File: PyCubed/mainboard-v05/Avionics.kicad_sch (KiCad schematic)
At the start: 33 parts, among them SW1 KMR231NG LFS, U1 MAX706RESA, U2 ATSAMD51J19A-AU, U3 BMX160, Y1 32.768kHz

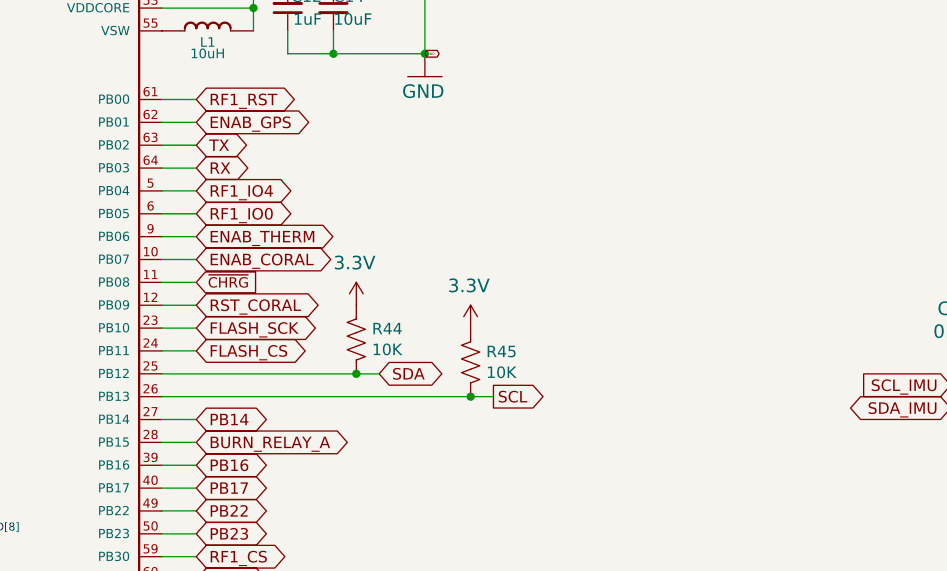
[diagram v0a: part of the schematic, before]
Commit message: final updates after JLC i2c error
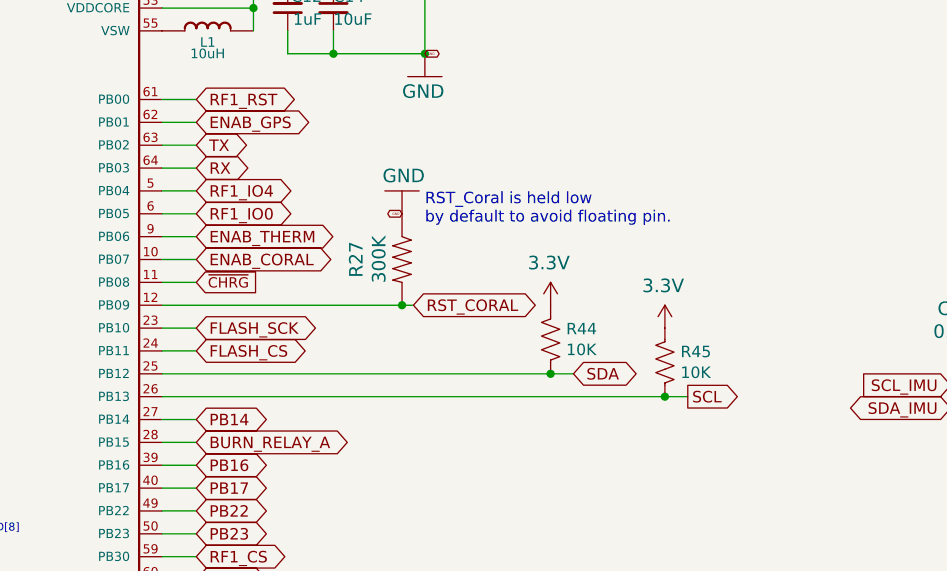
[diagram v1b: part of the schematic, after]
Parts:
- added R27: 300K, Resistor_SMD:R_0603_1608Metric, symbol mainboard:R-US_R0603
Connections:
- net GND: now also R27.1
- net RST_CORAL: now also R27.2
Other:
- note added: "RST_Coral is held low by default to avoid floating pin."
- moved on the sheet: R44, R45

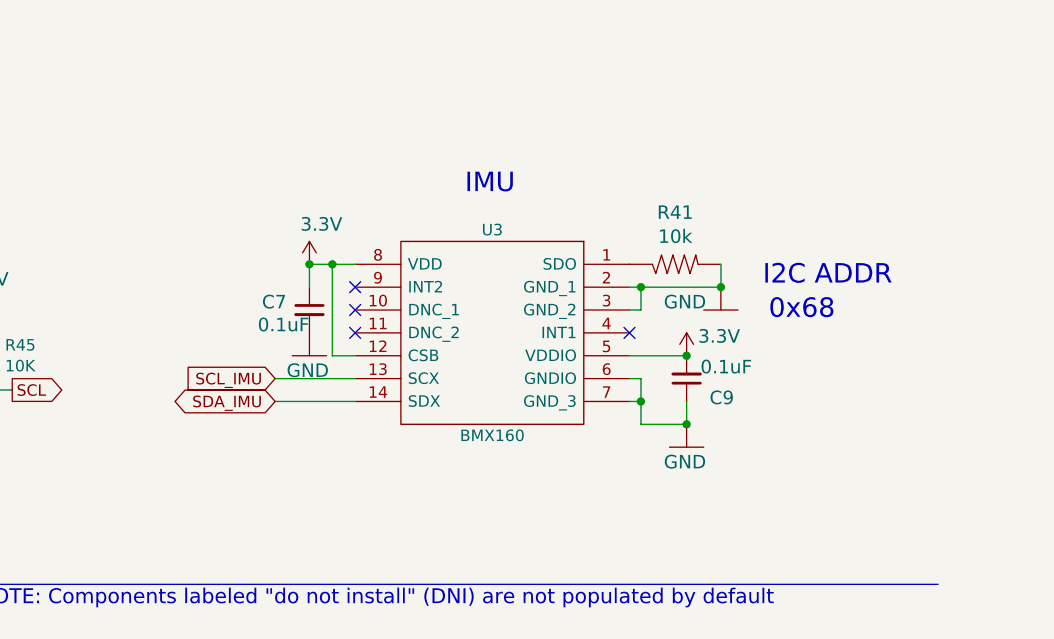
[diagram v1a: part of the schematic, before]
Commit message: add replacement sensors
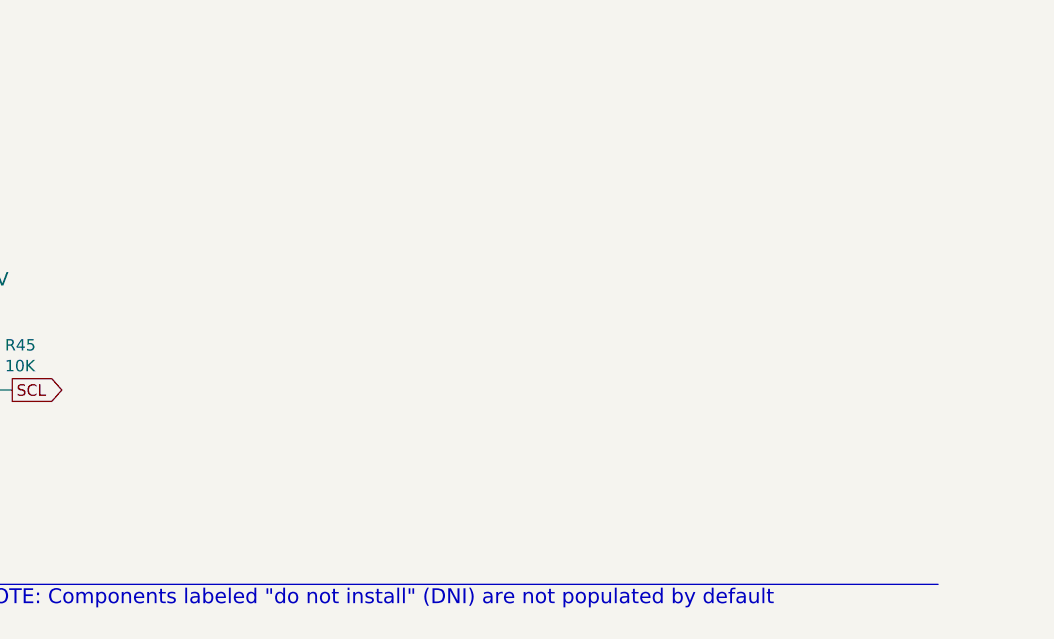
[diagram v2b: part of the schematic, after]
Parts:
- removed C7, C9: 0.1uF, Capacitor_SMD:C_0603_1608Metric, symbol mainboard:C_Small
- removed R41: 10k, Resistor_SMD:R_0603_1608Metric, symbol mainboard:R-US_R0603
- removed U3: BMX160, mainboard:BMX160, symbol mainboard:BMX160
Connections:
- no-connect marks 6 -> 2
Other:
- note removed: "0x68"
- note removed: "I2C ADDR"
- note removed: "IMU"
